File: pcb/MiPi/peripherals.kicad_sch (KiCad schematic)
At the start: 18 parts, among them Q1 Si1308EDL

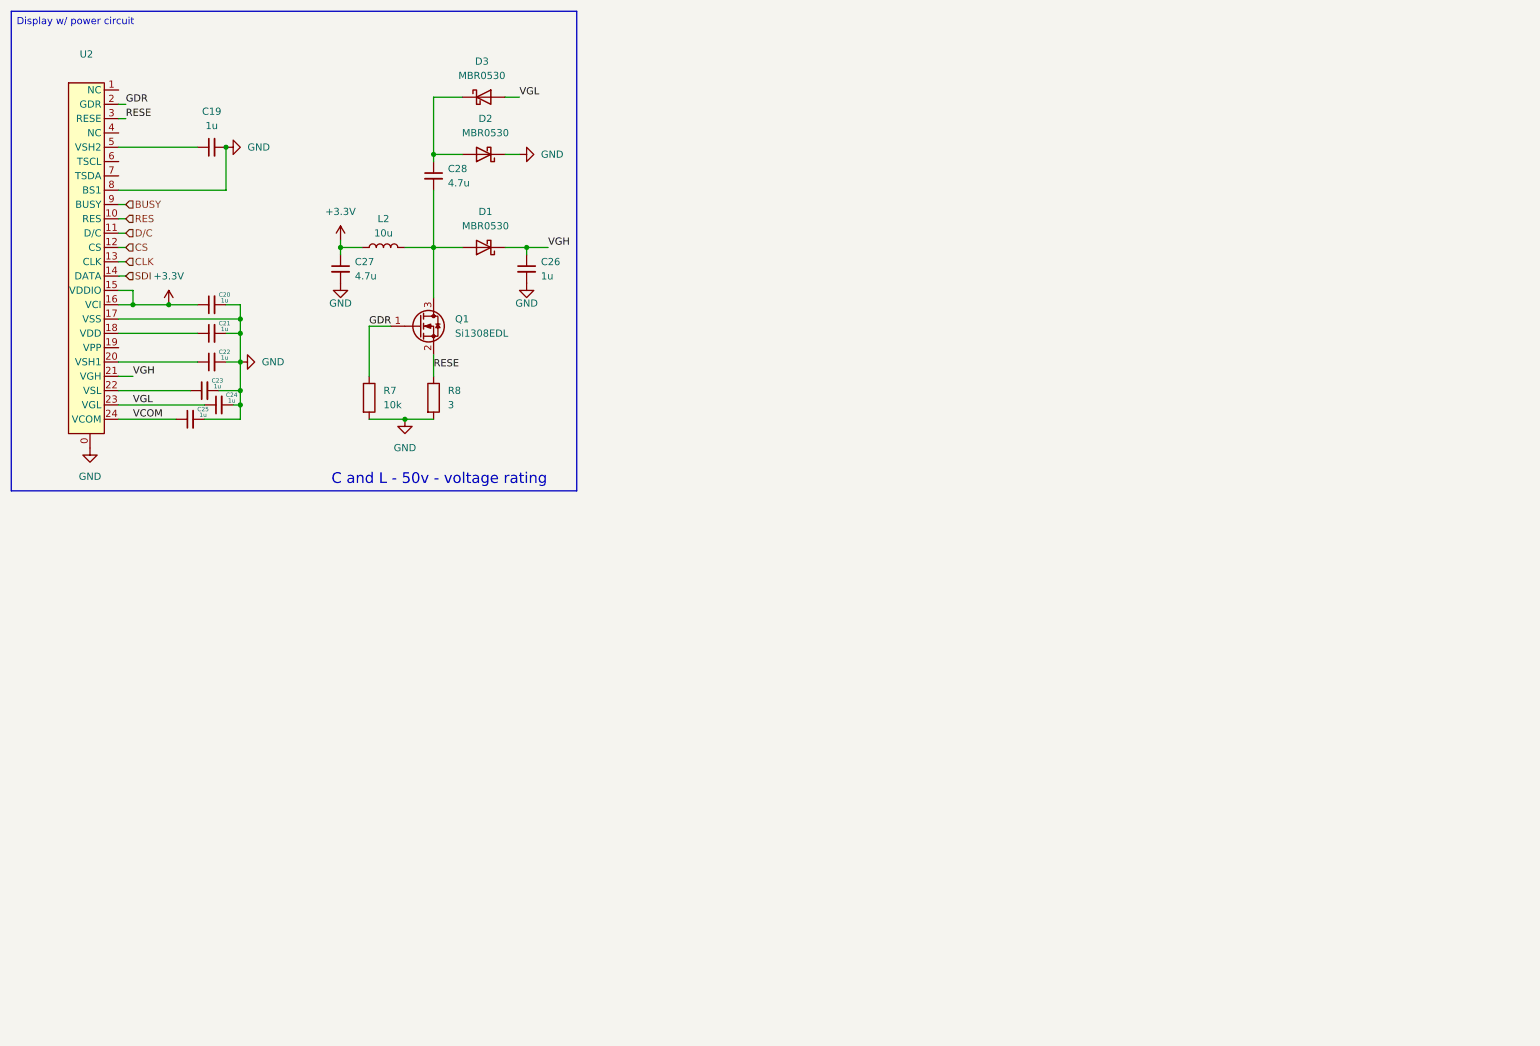
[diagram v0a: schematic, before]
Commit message: Did RDA5807M, controls and SD circuit schematic
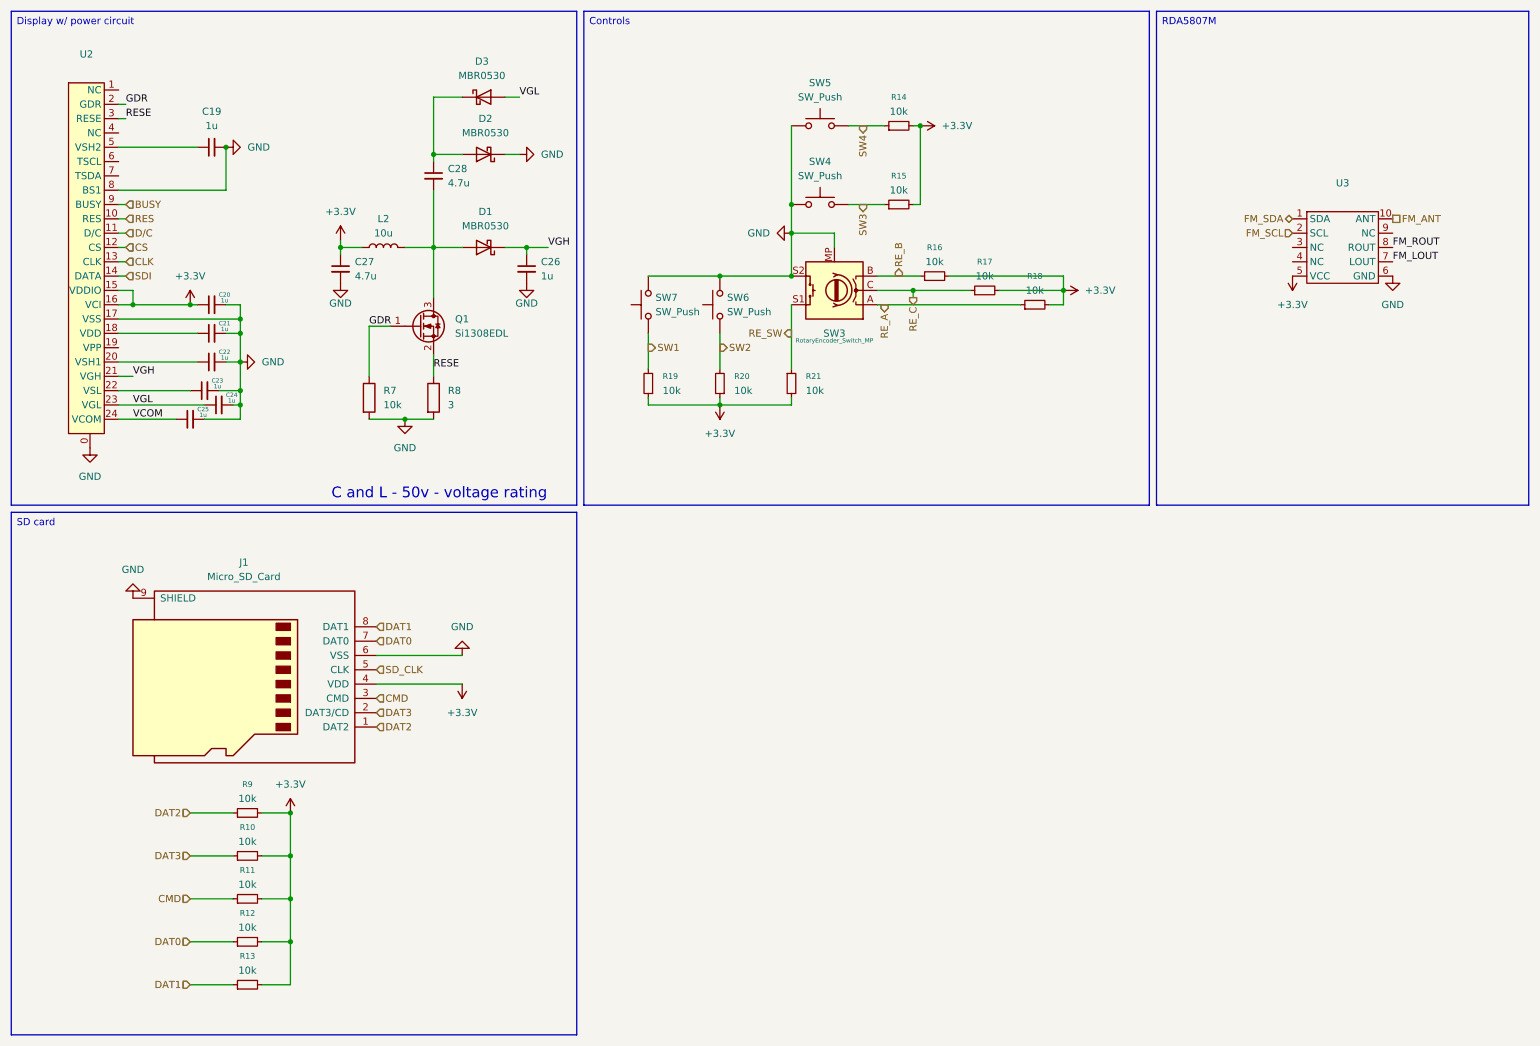
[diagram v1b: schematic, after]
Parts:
- added J1: Micro_SD_Card, symbol Connector:Micro_SD_Card
- added R10, R11, R12, R13, R14, R15, R16, R17, R18, R19, R20, R21, R9: 10k, symbol Device:R_Small
- added SW3: RotaryEncoder_Switch_MP, symbol Device:RotaryEncoder_Switch_MP
- added SW4, SW5, SW6, SW7: SW_Push, symbol Switch:SW_Push
- added U3: ~, symbol USER Library:RDA5807M_module
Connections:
- net +3.3V: now also J1.4 (VDD), R10.2, R11.2, R12.2, R13.2, R14.2, R15.2, R16.2, R17.2, R18.2, R19.1, R20.1, R21.2, R9.2, U3.5 (VCC)
- net GND: now also J1.6 (VSS), J1.9 (SHIELD), SW3.MP, SW3.S2, SW4.1, SW5.1, SW6.2, SW7.2, U3.6 (GND)
- new net CMD: J1.3 (CMD), R11.1
- new net DAT0: J1.7 (DAT0), R12.1
- new net DAT1: J1.8 (DAT1), R13.1
- new net DAT2: J1.1 (DAT2), R9.1
- new net DAT3: J1.2 (DAT3/CD), R10.1
- new net FM_ANT: U3.10 (ANT)
- new net FM_LOUT: U3.7 (LOUT)
- new net FM_ROUT: U3.8 (ROUT)
- new net FM_SCL: U3.2 (SCL)
- new net FM_SDA: U3.1 (SDA)
- new net RE_A: R18.1, SW3.A
- new net RE_B: R16.1, SW3.B
- new net RE_C: R17.1, SW3.C
- new net RE_SW: R21.1, SW3.S1
- new net SD_CLK: J1.5 (CLK)
- new net SW1: R19.2, SW7.1
- new net SW2: R20.2, SW6.1
- new net SW3: R15.1, SW4.2
- new net SW4: R14.1, SW5.2

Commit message: Peripherals sheet basically finished; Needs a check.
Added an analog switch for selecting between the radio audio and the RP2350's audio; A headphone audio amp and an audio jack
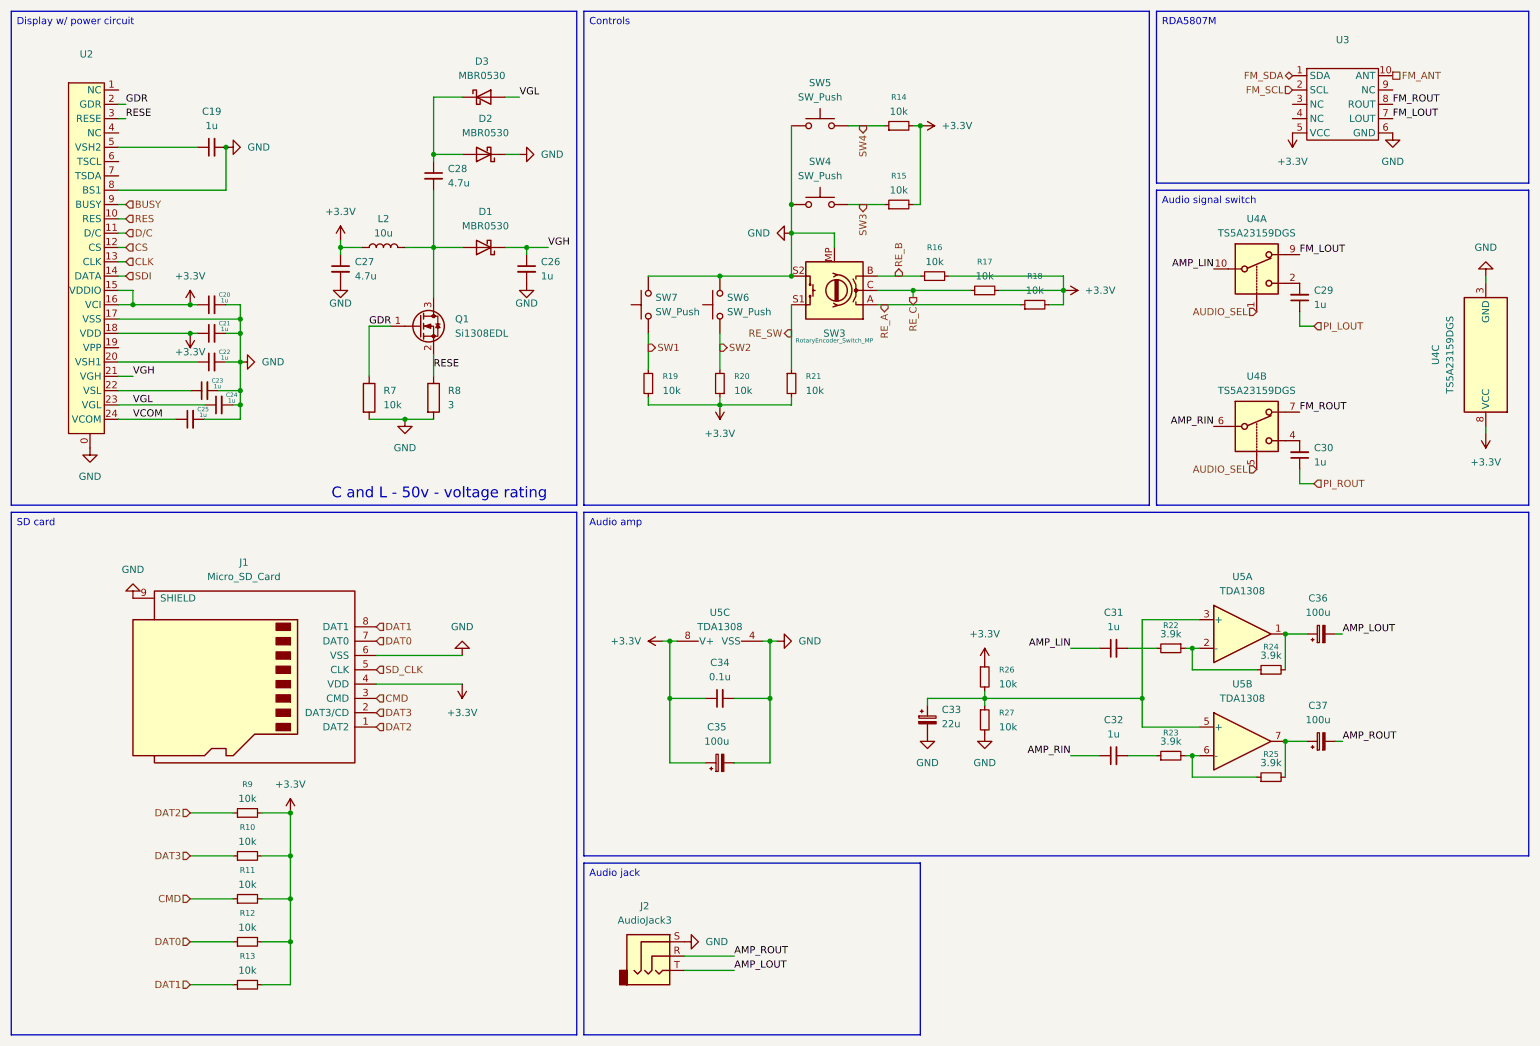
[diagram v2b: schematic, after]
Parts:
- added C29, C30, C31, C32: 1u, symbol Device:C_Small
- added C33: 22u, symbol Device:C_Polarized_Small
- added C34: 0.1u, symbol Device:C_Small
- added C35, C36, C37: 100u, symbol Device:C_Polarized_Small
- added J2: AudioJack3, symbol Connector_Audio:AudioJack3
- added R22, R23, R24, R25: 3.9k, symbol Device:R_Small
- added R26, R27: 10k, symbol Device:R_Small
- added U4: TS5A23159DGS, Package_SO:VSSOP-10_3x3mm_P0.5mm, symbol Analog_Switch:TS5A23159DGS
- added U5: TDA1308, symbol Amplifier_Audio:TDA1308
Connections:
- net +3.3V: now also C21.1, U2.18 (VDD), C34.1, C35.1, R26.1, U4.8 (VCC), U5.8 (V+)
- net FM_LOUT: now also U4.9
- net FM_ROUT: now also U4.7
- net GND: now also C33.2, C34.2, C35.2, J2.S, R27.2, U4.3 (GND), U5.4 (VSS)
- new net: R22.1, R24.1, U5.2 (-)
- new net: C31.2, R22.2
- new net: R23.2, R25.1, U5.6 (-)
- new net: C37.1, R25.2, U5.7
- new net: C33.1, R26.2, R27.1, U5.3 (+), U5.5 (+)
- new net: C36.1, R24.2, U5.1
- new net: C32.2, R23.1
- new net: C30.2, U4.4
- new net: C29.2, U4.2
- new net AMP_LIN: C31.1, U4.10
- new net AMP_LOUT: C36.2, J2.T
- new net AMP_RIN: C32.1, U4.6
- new net AMP_ROUT: C37.2, J2.R
- new net AUDIO_SEL: U4.1, U4.5
- new net PI_LOUT: C29.1
- new net PI_ROUT: C30.1
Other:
- company: (none) -> Christian Spînu
- moved on the sheet: U3

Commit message: Started routing the PCB
Done with the RP2350's decoupling caps, buttons and USB-C connector; Done with the display's driving circuit.
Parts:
- C19, C20, C21, C22, C23, C24, C25, C26, C27, C28, C29, C30, C31, C32, C33, C34: footprint (none) -> Capacitor_SMD:C_0402_1005Metric
- C35, C36, C37: footprint (none) -> Capacitor_SMD:C_1206_3216Metric
- J1: footprint (none) -> Connector_Card:microSD_HC_Hirose_DM3D-SF
- J2: footprint (none) -> Connector_Audio:Jack_3.5mm_CUI_SJ-3523-SMT_Horizontal
- L2: footprint (none) -> Inductor_SMD:L_1206_3216Metric
- R10, R11, R12, R13, R14, R15, R16, R17, R18, R19, R20, R21, R22, R23, R24, R25, R26, R27, R7, R8, R9: footprint (none) -> Resistor_SMD:R_0402_1005Metric
- SW3: footprint (none) -> Rotary_Encoder:RotaryEncoder_Alps_EC11E-Switch_Vertical_H20mm
- SW4, SW5, SW6, SW7: footprint (none) -> Button_Switch_SMD:SW_Push_1P1T_NO_CK_KMR2
- U2: footprint (none) -> USER Library:FPC_24_TOP_CONTACTS
- U3: footprint (none) -> USER Library:RDA5807M module
- U5: footprint (none) -> Package_SO:SOIC-8_3.9x4.9mm_P1.27mm
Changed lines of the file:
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@@
 			)
 		)
-		(property "Footprint" ""
+		(property "Footprint" "Resistor_SMD:R_0402_1005Metric"
 			(at 219.71 127 0)
 			(effects
@@
 			)
 		)
-		(property "Footprint" ""
+		(property "Footprint" "Resistor_SMD:R_0402_1005Metric"
 			(at 55.88 163.83 0)
 			(effects
@@
 			)
 		)
-		(property "Footprint" ""
+		(property "Footprint" "Button_Switch_SMD:SW_Push_1P1T_NO_CK_KMR2"
 			(at 134.62 66.04 0)
 			(effects
@@
 			)
 		)
-		(property "Footprint" ""
+		(property "Footprint" "Capacitor_SMD:C_0402_1005Metric"
 			(at 88.9 43.18 0)
 			(effects
@@
 			)
 		)
-		(property "Footprint" ""
+		(property "Footprint" "Capacitor_SMD:C_0402_1005Metric"
 			(at 49.53 76.2 0)
 			(effects
@@
 			)
 		)
-		(property "Footprint" ""
+		(property "Footprint" "Resistor_SMD:R_0402_1005Metric"
 			(at 237.49 149.86 0)
 			(effects
@@
 			)
 		)
-		(property "Footprint" ""
+		(property "Footprint" "Resistor_SMD:R_0402_1005Metric"
 			(at 186.69 139.7 0)
 			(effects
@@
 			)
 		)
-		(property "Footprint" ""
+		(property "Footprint" "Resistor_SMD:R_0402_1005Metric"
 			(at 152.4 80.01 0)
 			(effects
@@
 			)
 		)
-		(property "Footprint" ""
+		(property "Footprint" "Resistor_SMD:R_0402_1005Metric"
 			(at 55.88 179.07 0)
 			(effects
@@
 			)
 		)
-		(property "Footprint" ""
+		(property "Footprint" "Resistor_SMD:R_0402_1005Metric"
 			(at 171.45 48.26 0)
 			(effects
@@
 			)
 		)
-		(property "Footprint" ""
+		(property "Footprint" "Capacitor_SMD:C_1206_3216Metric"
 			(at 139.7 147.32 0)
 			(effects
@@
 			)
 		)
-		(property "Footprint" ""
+		(property "Footprint" "Resistor_SMD:R_0402_1005Metric"
 			(at 55.88 156.21 0)
 			(effects
@@
 			)
 		)
-		(property "Footprint" ""
+		(property "Footprint" "Package_SO:SOIC-8_3.9x4.9mm_P1.27mm"
 			(at 232.41 124.46 0)
 			(effects
@@
 			)
 		)
-		(property "Footprint" ""
+		(property "Footprint" "Capacitor_SMD:C_0402_1005Metric"
 			(at 49.53 38.1 0)
 			(effects
@@
 			)
 		)
-		(property "Footprint" ""
+		(property "Footprint" "Capacitor_SMD:C_0402_1005Metric"
 			(at 105.41 59.69 0)
 			(effects
@@
 			)
 		)
-		(property "Footprint" ""
+		(property "Footprint" "Package_SO:SOIC-8_3.9x4.9mm_P1.27mm"
 			(at 232.41 143.51 0)
 			(effects
@@
 			)
 		)
-		(property "Footprint" ""
+		(property "Footprint" "Capacitor_SMD:C_0402_1005Metric"
 			(at 209.55 146.05 0)
 			(effects
@@
 			)
 		)
-		(property "Footprint" ""
+		(property "Footprint" "Button_Switch_SMD:SW_Push_1P1T_NO_CK_KMR2"
 			(at 157.48 43.18 0)
 			(effects
@@
 			)
 		)
-		(property "Footprint" ""
+		(property "Footprint" "Capacitor_SMD:C_0402_1005Metric"
 			(at 49.53 66.04 0)
 			(effects
@@
 			)
 		)
-		(property "Footprint" ""
+		(property "Footprint" "Resistor_SMD:R_0402_1005Metric"
 			(at 186.69 132.08 0)
 			(effects
@@
 			)
 		)
-		(property "Footprint" ""
+		(property "Footprint" "Resistor_SMD:R_0402_1005Metric"
 			(at 219.71 146.05 0)
 			(effects
@@
 			)
 		)
-		(property "Footprint" ""
+		(property "Footprint" "Capacitor_SMD:C_0402_1005Metric"
 			(at 72.39 59.69 0)
 			(effects
@@
 			)
 		)
-		(property "Footprint" ""
+		(property "Footprint" "Resistor_SMD:R_0402_1005Metric"
 			(at 237.49 130.81 0)
 			(effects
@@
 			)
 		)
-		(property "Footprint" ""
+		(property "Footprint" "Resistor_SMD:R_0402_1005Metric"
 			(at 127 80.01 0)
 			(effects
@@
 			)
 		)
-		(property "Footprint" ""
+		(property "Footprint" "Resistor_SMD:R_0402_1005Metric"
 			(at 171.45 34.29 0)
 			(effects
@@
 			)
 		)
-		(property "Footprint" ""
+		(property "Footprint" "Resistor_SMD:R_0402_1005Metric"
 			(at 75.692 82.55 90)
 			(effects
@@
 			)
 		)
-		(property "Footprint" ""
+		(property "Footprint" "Resistor_SMD:R_0402_1005Metric"
 			(at 55.88 171.45 0)
 			(effects
@@
 			)
 		)
-		(property "Footprint" ""
+		(property "Footprint" "Resistor_SMD:R_0402_1005Metric"
 			(at 195.58 66.04 0)
 			(effects
@@
 			)
 		)
-		(property "Footprint" ""
+		(property "Footprint" "Inductor_SMD:L_1206_3216Metric"
 			(at 80.01 55.88 0)
 			(effects
@@
 			)
 		)
-		(property "Footprint" ""
+		(property "Footprint" "Button_Switch_SMD:SW_Push_1P1T_NO_CK_KMR2"
 			(at 157.48 29.21 0)
 			(effects
@@
 			)
 		)
-		(property "Footprint" ""
+		(property "Footprint" "Capacitor_SMD:C_0402_1005Metric"
 			(at 209.55 127 0)
 			(effects
@@
 			)
 		)
-		(property "Footprint" ""
+		(property "Footprint" "Capacitor_SMD:C_0402_1005Metric"
 			(at 242.57 64.77 0)
 			(effects
@@
 			)
 		)
-		(property "Footprint" ""
+		(property "Footprint" "Capacitor_SMD:C_1206_3216Metric"
 			(at 246.38 143.51 0)
 			(effects
@@
 			)
 		)
-		(property "Footprint" ""
+		(property "Footprint" "Button_Switch_SMD:SW_Push_1P1T_NO_CK_KMR2"
 			(at 121.92 66.04 0)
 			(effects
@@
 			)
 		)
-		(property "Footprint" ""
+		(property "Footprint" "Capacitor_SMD:C_1206_3216Metric"
 			(at 246.38 124.46 0)
 			(effects
@@
 			)
 		)
-		(property "Footprint" ""
+		(property "Footprint" "Connector_Card:microSD_HC_Hirose_DM3D-SF"
 			(at 26.67 140.97 0)
 			(effects
@@
 			)
 		)
-		(property "Footprint" ""
+		(property "Footprint" "Resistor_SMD:R_0402_1005Metric"
 			(at 186.69 63.5 0)
 			(effects
@@
 			)
 		)
-		(property "Footprint" ""
+		(property "Footprint" "Capacitor_SMD:C_0402_1005Metric"
 			(at 176.53 139.7 0)
 			(effects
@@
 			)
 		)
-		(property "Footprint" ""
+		(property "Footprint" "Capacitor_SMD:C_0402_1005Metric"
 			(at 45.72 86.36 0)
 			(effects
@@
 			)
 		)
-		(property "Footprint" ""
+		(property "Footprint" "USER Library:RDA5807M module"
 			(at 250.19 30.48 0)
 			(effects
@@
 			)
 		)
-		(property "Footprint" ""
+		(property "Footprint" "USER Library:FPC_24_TOP_CONTACTS"
 			(at 29.21 38.1 0)
 			(effects
@@
 			)
 		)
-		(property "Footprint" ""
+		(property "Footprint" "Connector_Audio:Jack_3.5mm_CUI_SJ-3523-SMT_Horizontal"
 			(at 128.27 181.61 0)
 			(effects
@@
 			)
 		)
-		(property "Footprint" ""
+		(property "Footprint" "Rotary_Encoder:RotaryEncoder_Alps_EC11E-Switch_Vertical_H20mm"
 			(at 163.83 67.564 0)
 			(effects
@@
 			)
 		)
-		(property "Footprint" ""
+		(property "Footprint" "Resistor_SMD:R_0402_1005Metric"
 			(at 177.8 60.96 0)
 			(effects
@@
 			)
 		)
-		(property "Footprint" ""
+		(property "Footprint" "Resistor_SMD:R_0402_1005Metric"
 			(at 55.88 186.69 0)
 			(effects
@@
 			)
 		)
-		(property "Footprint" ""
+		(property "Footprint" "Capacitor_SMD:C_0402_1005Metric"
 			(at 50.8 83.82 0)
 			(effects
@@
 			)
 		)
-		(property "Footprint" ""
+		(property "Footprint" "Capacitor_SMD:C_0402_1005Metric"
 			(at 242.57 92.71 0)
 			(effects
@@
 			)
 		)
-		(property "Footprint" ""
+		(property "Footprint" "Resistor_SMD:R_0402_1005Metric"
 			(at 139.7 80.01 0)
 			(effects
@@
 			)
 		)
-		(property "Footprint" ""
+		(property "Footprint" "Capacitor_SMD:C_0402_1005Metric"
 			(at 48.26 81.28 0)
 			(effects
@@
 			)
 		)
-		(property "Footprint" ""
+		(property "Footprint" "Capacitor_SMD:C_0402_1005Metric"
 			(at 49.53 71.12 0)
 			(effects
@@
 			)
 		)
-		(property "Footprint" ""
+		(property "Footprint" "Package_SO:SOIC-8_3.9x4.9mm_P1.27mm"
 			(at 139.7 123.19 0)
 			(effects
@@
 			)
 		)
-		(property "Footprint" ""
+		(property "Footprint" "Capacitor_SMD:C_0402_1005Metric"
 			(at 139.7 135.89 0)
 			(effects
@@
 			)
 		)
-		(property "Footprint" ""
+		(property "Footprint" "Resistor_SMD:R_0402_1005Metric"
 			(at 87.122 82.55 90)
 			(effects

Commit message: Made the Gerbers, BOM, and CDL for the first version of miPi
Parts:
- C19, C20, C21, C22, C23, C24, C25, C26, C29, C30, C31, C32: LCSC (none) -> C29266
- C27, C28: LCSC (none) -> C23733
- C33: LCSC (none) -> C105226
- C34: LCSC (none) -> C1525
- C35, C36, C37: LCSC (none) -> C15008
- D1, D2, D3: LCSC (none) -> C18863
- J1: LCSC (none) -> C719027
- J2: LCSC (none) -> C4991872
- L2: LCSC (none) -> C1051
- Q1: LCSC (none) -> C4355112
- R10, R11, R12, R13, R14, R15, R16, R17, R18, R19, R20, R21, R26, R27, R7, R9: LCSC (none) -> C71617
- R22, R23, R24, R25: LCSC (none) -> C278582
- R8: LCSC (none) -> C400520
- SW3: LCSC (none) -> C202365
- SW4, SW5, SW6, SW7: LCSC (none) -> C269272
- U2: LCSC (none) -> C22751583
- U3: now left out of the parts list
- U4: LCSC (none) -> C42751
- U5: LCSC (none) -> C38340
